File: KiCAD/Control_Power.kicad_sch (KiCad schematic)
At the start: 8 parts, among them J1 DIN-40-Female, U1 ADPL40505A

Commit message: Finished routing
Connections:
- net ADC1_CS: now also J1.17; no longer J1.16
- net ADC1_nEOC: now also J1.37; no longer J1.19
- net ADC2_CS: now also J1.39; no longer J1.17
- net ADC2_nEOC: now also J1.40; no longer J1.20
- net ADC_CONVST: now also J1.38; no longer J1.18
- net ADC_CR0: now also J1.36; no longer J1.23
- net ADC_CR1: now also J1.35; no longer J1.24
- net ADC_DB0/CR2: now also J1.34; no longer J1.25
- net ADC_DB10: now also J1.22; no longer J1.37
- net ADC_DB11: now also J1.21; no longer J1.38
- net ADC_DB12: now also J1.20; no longer J1.39
- net ADC_DB13: now also J1.19; no longer J1.40
- net ADC_DB1/CR3: now also J1.33; no longer J1.26
- net ADC_DB2: now also J1.32; no longer J1.27
- net ADC_DB3: now also J1.31; no longer J1.28
- net ADC_DB4: now also J1.28; no longer J1.31
- net ADC_DB5: now also J1.27; no longer J1.32
- net ADC_DB6: now also J1.26; no longer J1.33
- net ADC_DB7: now also J1.25; no longer J1.34
- net ADC_DB8: now also J1.24; no longer J1.35
- net ADC_DB9: now also J1.23; no longer J1.36
- net ADC_nRD: now also J1.18; no longer J1.21
- net ADC_nWR: now also J1.16; no longer J1.22
- net PA_ENABLE: now also J1.2; no longer J1.4
- net PWM: now also J1.4; no longer J1.2
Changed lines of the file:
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@@
 	(hierarchical_label "ADC_DB8"
 		(shape bidirectional)
-		(at 66.04 106.68 180)
-		(effects
-			(font
-				(size 1.27 1.27)
-			)
-			(justify right)
+		(at 91.44 91.44 0)
+		(effects
+			(font
+				(size 1.27 1.27)
+			)
+			(justify left)
 		)
 	)
 	(hierarchical_label "PWM"
 		(shape output)
-		(at 91.44 63.5 0)
+		(at 91.44 66.04 0)
 		(effects
 			(font
@@
 	(hierarchical_label "ADC1_CS"
 		(shape output)
-		(at 91.44 81.28 0)
-		(effects
-			(font
-				(size 1.27 1.27)
-			)
-			(justify left)
+		(at 66.04 83.82 180)
+		(effects
+			(font
+				(size 1.27 1.27)
+			)
+			(justify right)
 		)
 	)
 	(hierarchical_label "ADC_DB7"
 		(shape bidirectional)
-		(at 91.44 104.14 0)
-		(effects
-			(font
-				(size 1.27 1.27)
-			)
-			(justify left)
+		(at 66.04 93.98 180)
+		(effects
+			(font
+				(size 1.27 1.27)
+			)
+			(justify right)
 		)
 	)
 	(hierarchical_label "ADC_DB9"
 		(shape bidirectional)
-		(at 91.44 106.68 0)
-		(effects
-			(font
-				(size 1.27 1.27)
-			)
-			(justify left)
+		(at 66.04 91.44 180)
+		(effects
+			(font
+				(size 1.27 1.27)
+			)
+			(justify right)
 		)
 	)
 	(hierarchical_label "ADC2_nEOC"
 		(shape input)
-		(at 91.44 86.36 0)
+		(at 91.44 111.76 0)
 		(effects
 			(font
@@
 	(hierarchical_label "ADC2_CS"
 		(shape output)
-		(at 66.04 83.82 180)
+		(at 66.04 111.76 180)
 		(effects
 			(font
@@
 	(hierarchical_label "ADC_DB5"
 		(shape bidirectional)
+		(at 66.04 96.52 180)
+		(effects
+			(font
+				(size 1.27 1.27)
+			)
+			(justify right)
+		)
+	)
+	(hierarchical_label "ADC_DB2"
+		(shape bidirectional)
 		(at 91.44 101.6 0)
 		(effects
@@
 		)
 	)
-	(hierarchical_label "ADC_DB2"
-		(shape bidirectional)
-		(at 66.04 96.52 180)
-		(effects
-			(font
-				(size 1.27 1.27)
-			)
-			(justify right)
-		)
-	)
 	(hierarchical_label "ADC_DB0{slash}CR2"
 		(shape bidirectional)
-		(at 66.04 93.98 180)
-		(effects
-			(font
-				(size 1.27 1.27)
-			)
-			(justify right)
+		(at 91.44 104.14 0)
+		(effects
+			(font
+				(size 1.27 1.27)
+			)
+			(justify left)
 		)
 	)
 	(hierarchical_label "ADC_DB12"
 		(shape bidirectional)
-		(at 66.04 111.76 180)
-		(effects
-			(font
-				(size 1.27 1.27)
-			)
-			(justify right)
+		(at 91.44 86.36 0)
+		(effects
+			(font
+				(size 1.27 1.27)
+			)
+			(justify left)
 		)
 	)
 	(hierarchical_label "ADC_DB3"
 		(shape bidirectional)
+		(at 66.04 101.6 180)
+		(effects
+			(font
+				(size 1.27 1.27)
+			)
+			(justify right)
+		)
+	)
+	(hierarchical_label "ADC_DB4"
+		(shape bidirectional)
 		(at 91.44 96.52 0)
 		(effects
@@
 		)
 	)
-	(hierarchical_label "ADC_DB4"
-		(shape bidirectional)
-		(at 66.04 101.6 180)
-		(effects
-			(font
-				(size 1.27 1.27)
-			)
-			(justify right)
-		)
-	)
 	(hierarchical_label "ADC_DB10"
 		(shape bidirectional)
-		(at 66.04 109.22 180)
-		(effects
-			(font
-				(size 1.27 1.27)
-			)
-			(justify right)
+		(at 91.44 88.9 0)
+		(effects
+			(font
+				(size 1.27 1.27)
+			)
+			(justify left)
 		)
 	)
 	(hierarchical_label "ADC_CR0"
 		(shape bidirectional)
-		(at 66.04 91.44 180)
-		(effects
-			(font
-				(size 1.27 1.27)
-			)
-			(justify right)
+		(at 91.44 106.68 0)
+		(effects
+			(font
+				(size 1.27 1.27)
+			)
+			(justify left)
 		)
 	)
 	(hierarchical_label "ADC_DB1{slash}CR3"
 		(shape bidirectional)
+		(at 66.04 104.14 180)
+		(effects
+			(font
+				(size 1.27 1.27)
+			)
+			(justify right)
+		)
+	)
+	(hierarchical_label "ADC_DB6"
+		(shape bidirectional)
 		(at 91.44 93.98 0)
 		(effects
@@
 			)
 			(justify left)
-		)
-	)
-	(hierarchical_label "ADC_DB6"
-		(shape bidirectional)
-		(at 66.04 104.14 180)
-		(effects
-			(font
-				(size 1.27 1.27)
-			)
-			(justify right)
 		)
 	)
 	(hierarchical_label "ADC_CONVST"
 		(shape output)
-		(at 91.44 83.82 0)
+		(at 91.44 109.22 0)
 		(effects
 			(font
@@
 	(hierarchical_label "ADC_DB11"
 		(shape bidirectional)
-		(at 91.44 109.22 0)
-		(effects
-			(font
-				(size 1.27 1.27)
-			)
-			(justify left)
+		(at 66.04 88.9 180)
+		(effects
+			(font
+				(size 1.27 1.27)
+			)
+			(justify right)
 		)
 	)
 	(hierarchical_label "ADC_CR1"
 		(shape bidirectional)
-		(at 91.44 91.44 0)
-		(effects
-			(font
-				(size 1.27 1.27)
-			)
-			(justify left)
+		(at 66.04 106.68 180)
+		(effects
+			(font
+				(size 1.27 1.27)
+			)
+			(justify right)
 		)
 	)
 	(hierarchical_label "PA_ENABLE"
 		(shape output)
-		(at 91.44 66.04 0)
+		(at 91.44 63.5 0)
 		(effects
 			(font
@@
 	(hierarchical_label "ADC_nWR"
 		(shape output)
-		(at 91.44 88.9 0)
+		(at 91.44 81.28 0)
 		(effects
 			(font
@@
 	(hierarchical_label "ADC1_nEOC"
 		(shape input)
+		(at 66.04 109.22 180)
+		(effects
+			(font
+				(size 1.27 1.27)
+			)
+			(justify right)
+		)
+	)
+	(hierarchical_label "ADC_DB13"
+		(shape bidirectional)
 		(at 66.04 86.36 180)
 		(effects
@@
 			)
 			(justify right)
-		)
-	)
-	(hierarchical_label "ADC_DB13"
-		(shape bidirectional)
-		(at 91.44 111.76 0)
-		(effects
-			(font
-				(size 1.27 1.27)
-			)
-			(justify left)
 		)
 	)
 	(hierarchical_label "ADC_nRD"
 		(shape output)
-		(at 66.04 88.9 180)
-		(effects
-			(font
-				(size 1.27 1.27)
-			)
-			(justify right)
+		(at 91.44 83.82 0)
+		(effects
+			(font
+				(size 1.27 1.27)
+			)
+			(justify left)
 		)
 	)
@@
 		)
 		(property "Package" "TDFN-8"
-			(at 180.34 63.5 0)
-			(hide yes)
+			(at 180.34 99.06 0)
 			(show_name no)
 			(do_not_autoplace no)
@@
 		)
 		(property "DisplayValue" "DIN-40-Female"
-			(at 78.74 116.84 0)
-			(show_name no)
-			(do_not_autoplace no)
-			(effects
-				(font
-					(size 1.27 1.27)
-				)
-				(justify bottom)
+			(at 78.74 119.38 0)
+			(show_name no)
+			(do_not_autoplace no)
+			(effects
+				(font
+					(size 1.27 1.27)
+				)
 			)
 		)
 		(property "Package" "2x20 - 100mil"
 			(at 78.74 116.84 0)
-			(hide yes)
-			(show_name no)
-			(do_not_autoplace no)
+			(show_name no)
+			(do_not_autoplace no)

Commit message: Added a debug header
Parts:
- added J2: DIN-20, Connector_IDC:IDC-Header_2x10_P2.54mm_Vertical, symbol Connectors:DIN-20
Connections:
- net +3.3V: now also J2.20
- net +5V: now also J2.18
- net GND: now also J2.12, J2.14, J2.16, J2.2, J2.4, J2.6, J2.8
- net DEBUG1: now reaches J1.1
- net DEBUG1: now also J2.1
- net DEBUG8: now reaches J1.10
- net DEBUG8: now also J2.13
- net DEBUG9: now reaches J1.13
- net DEBUG9: now also J2.15
- net DEBUG10: now reaches J1.14
- net DEBUG10: now also J2.17
- net DEBUG11: now reaches J1.15
- net DEBUG11: now also J2.19
- net DEBUG2: now reaches J1.3
- net DEBUG2: now also J2.3
- net DEBUG3: now reaches J1.5
- net DEBUG3: now also J2.5
- net DEBUG4: now reaches J1.6
- net DEBUG4: now also J2.7
- net DEBUG5: now reaches J1.7
- net DEBUG5: now also J2.9
- net DEBUG6: now reaches J1.8
- net DEBUG6: now also J2.10
- net DEBUG7: now reaches J1.9
- net DEBUG7: now also J2.11

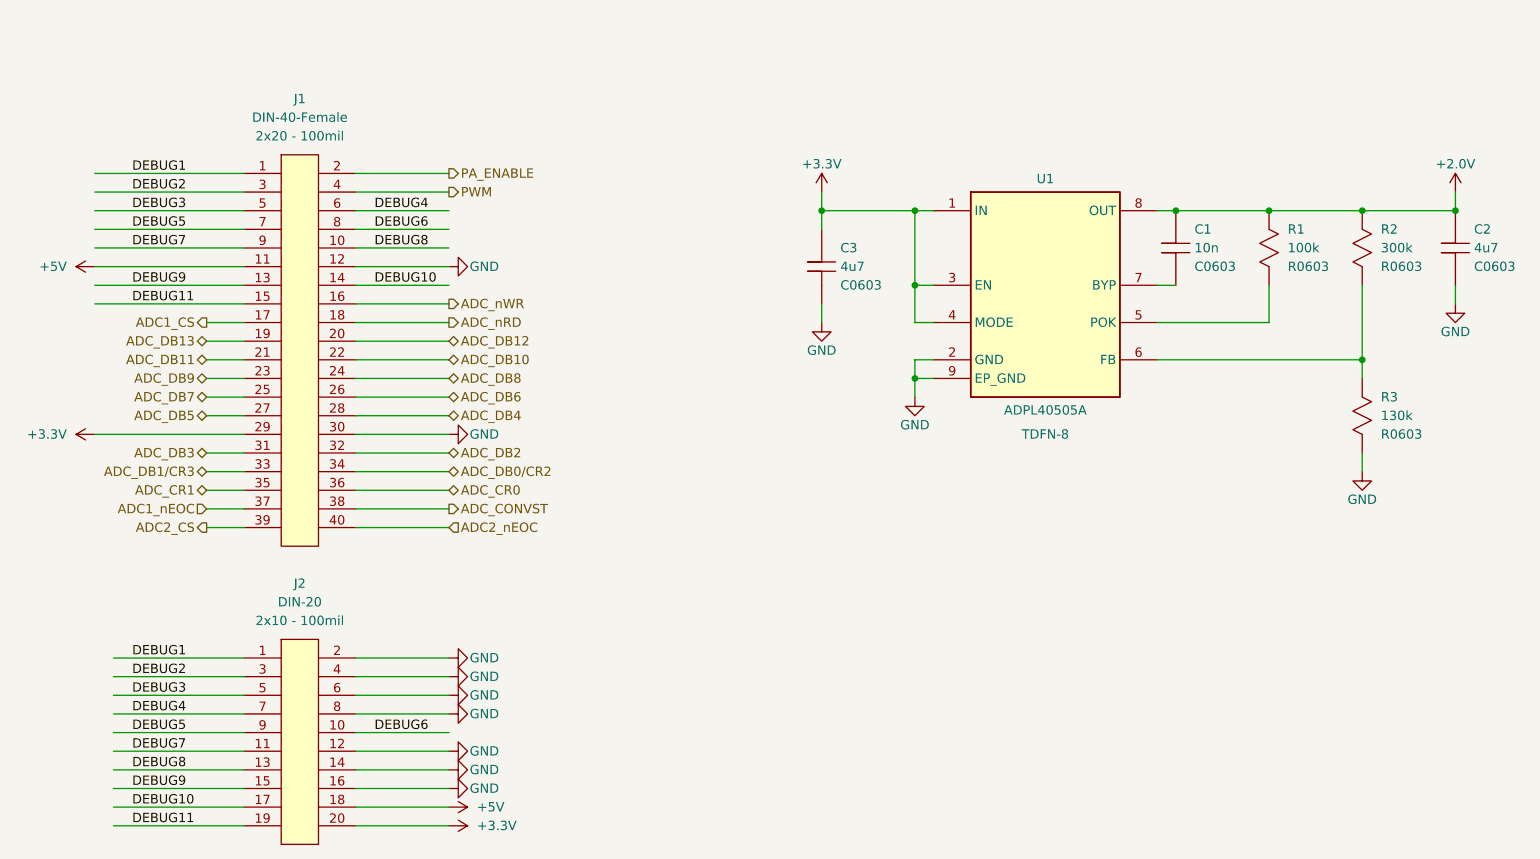
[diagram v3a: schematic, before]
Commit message: Added PA_Enable pull-down and moved the debug header
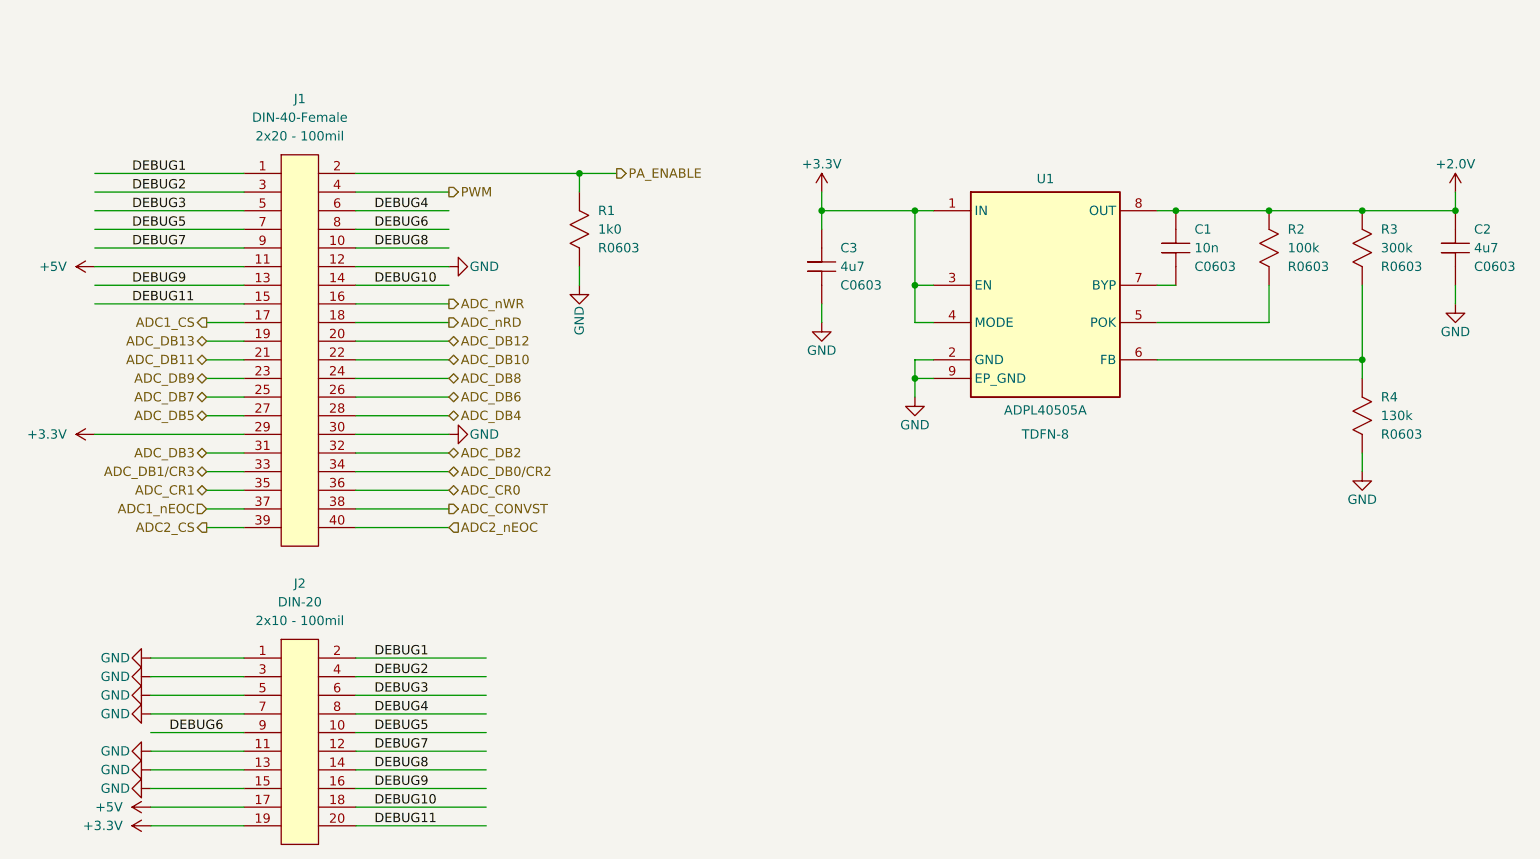
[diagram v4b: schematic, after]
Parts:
- added R1: R0603_1k0, Resistor_SMD:R_0603_1608Metric, symbol Resistors0603:R0603_1k0
- renumbered R1 to R2, R2 to R3, R3 to R4
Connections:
- net +3.3V: now also J2.19; no longer J2.20
- net +5V: now also J2.17; no longer J2.18
- net DEBUG1: now also J2.2; no longer J2.1
- net DEBUG10: now also J2.18; no longer J2.17
- net DEBUG11: now also J2.20; no longer J2.19
- net DEBUG2: now also J2.4; no longer J2.3
- net DEBUG3: now also J2.6; no longer J2.5
- net DEBUG4: now also J2.8; no longer J2.7
- net DEBUG5: now also J2.10; no longer J2.9
- net DEBUG6: now also J2.9; no longer J2.10
- net DEBUG7: now also J2.12; no longer J2.11
- net DEBUG8: now also J2.14; no longer J2.13
- net DEBUG9: now also J2.16; no longer J2.15
- net GND: now also J2.1, J2.11, J2.13, J2.15, J2.3, J2.5, J2.7, R1.2; no longer J2.12, J2.14, J2.16, J2.2, J2.4, J2.6, J2.8
- net PA_ENABLE: now also R1.1

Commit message: Moved the microphone RL to per-channel instead of per-mic
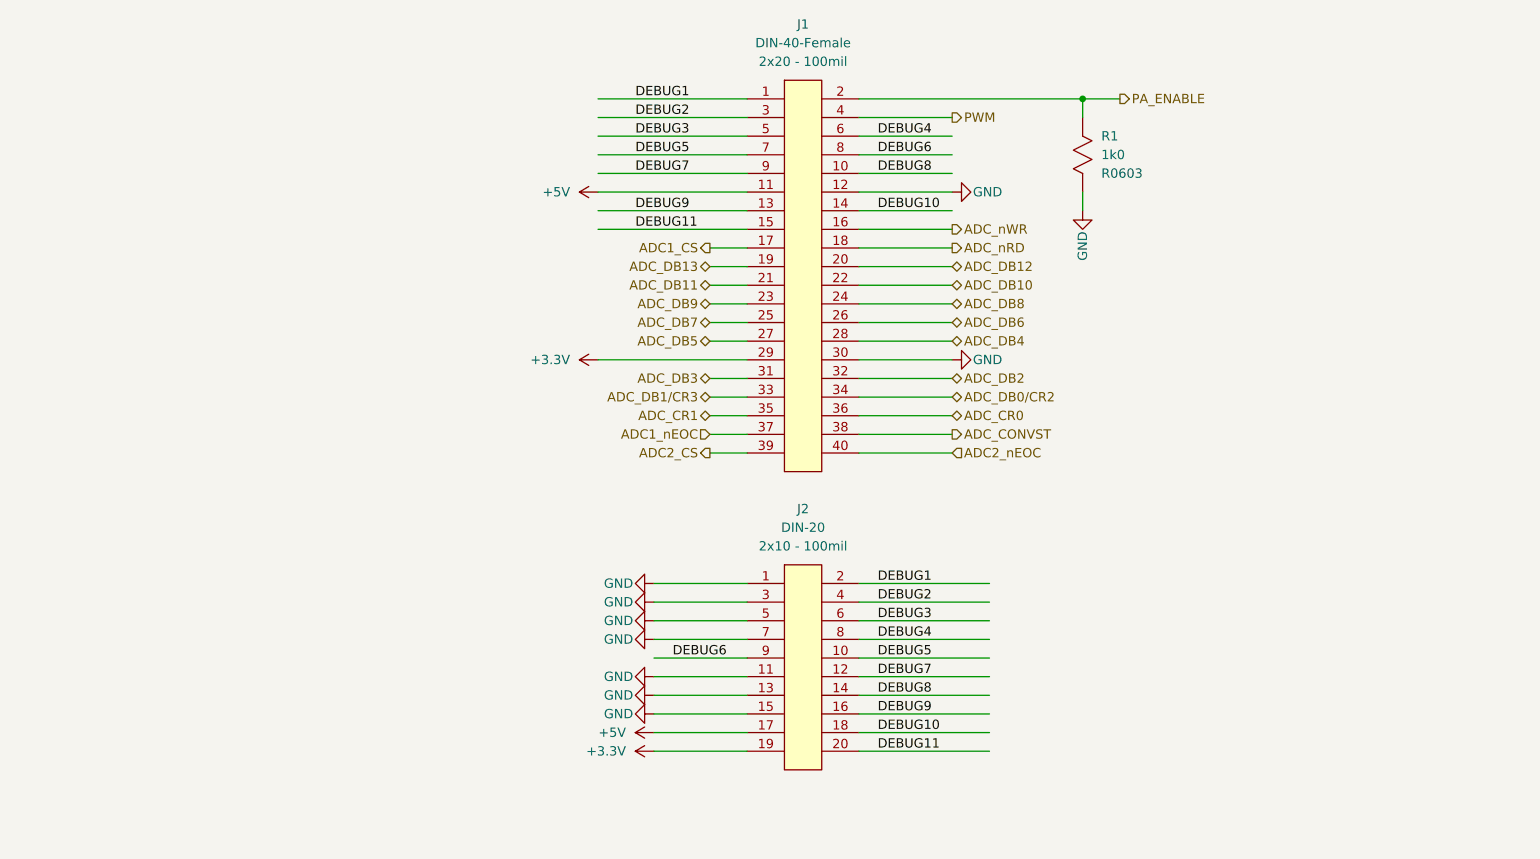
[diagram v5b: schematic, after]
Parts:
- removed C1: C0603_10n, Capacitor_SMD:C_0603_1608Metric, symbol Capacitors:C0603_10n
- removed C2, C3: C0603_4u7, Capacitor_SMD:C_0603_1608Metric, symbol Capacitors:C0603_4u7
- removed R2: R0603_100k, Resistor_SMD:R_0603_1608Metric, symbol Resistors0603:R0603_100k
- removed R3: R0603_300k, Resistor_SMD:R_0603_1608Metric, symbol Resistors0603:R0603_300k
- removed R4: R0603_130k, Resistor_SMD:R_0603_1608Metric, symbol Resistors0603:R0603_130k
- removed U1: ADPL40505A, SamacSys_Parts:SON50P200X200X80-9N-D, symbol Regulators:ADPL40505A
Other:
- moved on the sheet: J1, J2, R1

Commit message: Added title block and version text
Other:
- company: (none) -> University of Cape Town
- title: (none) -> Control and Power
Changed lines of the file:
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@@
 	(generator_version "10.0")
 	(paper "A4")
+	(title_block
+		(title "Control and Power")
+		(date "2026-05-09")
+		(rev "v1.0")
+		(company "University of Cape Town")
+	)
 	(junction
 		(at 185.42 53.34)

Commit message: Regenerated CAM output
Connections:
- net ADC1_CS renamed ADC1_nCS
- net ADC2_CS renamed ADC2_nCS
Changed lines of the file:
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@@
 		(rev "v1.0")
 		(company "University of Cape Town")
+		(comment 1 "Radar Remote Sensing Group")
+		(comment 2 "Radar Masters")
 	)
 	(junction
@@
 		)
 	)
-	(hierarchical_label "ADC1_CS"
+	(hierarchical_label "ADC1_nCS"
 		(shape output)
 		(at 134.62 73.66 180)
@@
 		)
 	)
-	(hierarchical_label "ADC2_CS"
+	(hierarchical_label "ADC2_nCS"
 		(shape output)
 		(at 134.62 101.6 180)
